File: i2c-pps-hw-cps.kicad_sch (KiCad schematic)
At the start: 36 parts, among them Q1 SiR880BDP, Q2 SiR880BDP, Q3 SiR880BDP, Q4 SiR880BDP, U1 BQ25758S

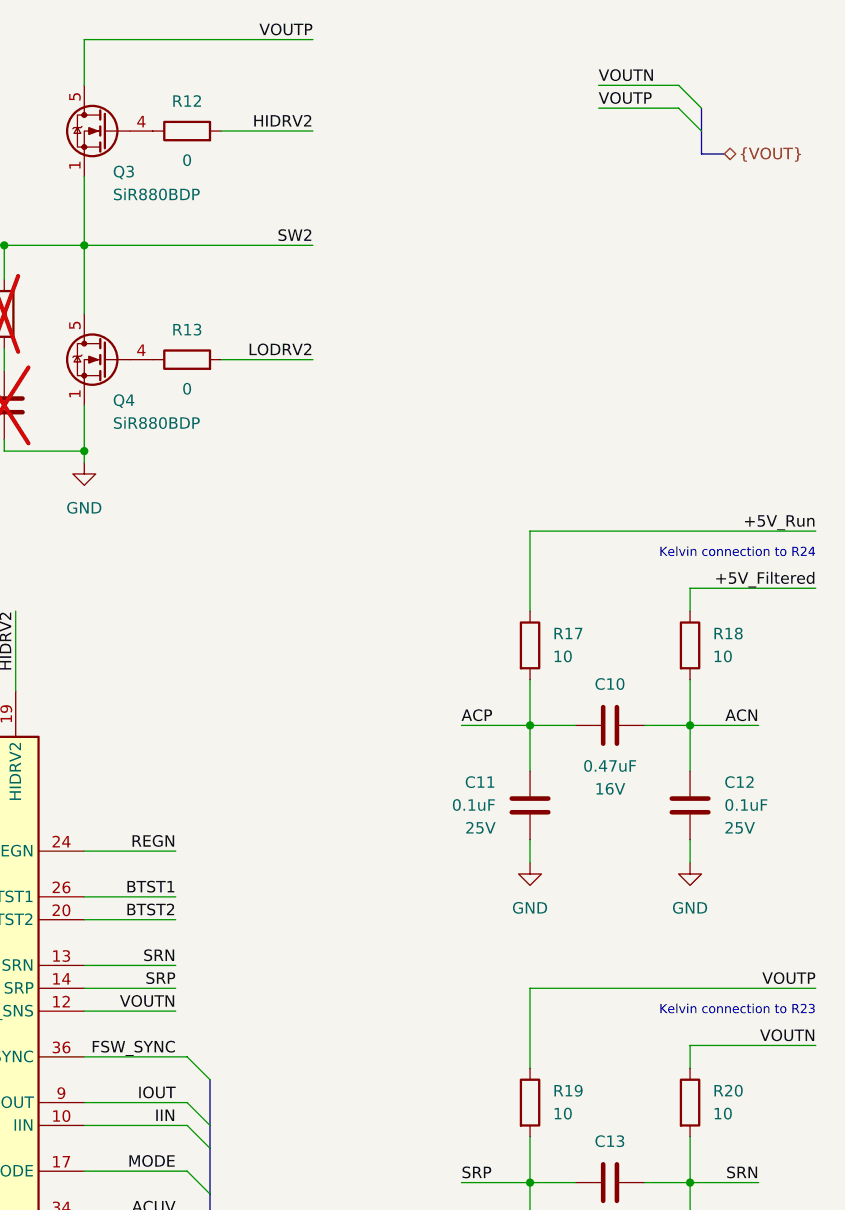
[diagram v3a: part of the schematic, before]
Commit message: Rename VOUTP to VOUT_Switcher for clarity
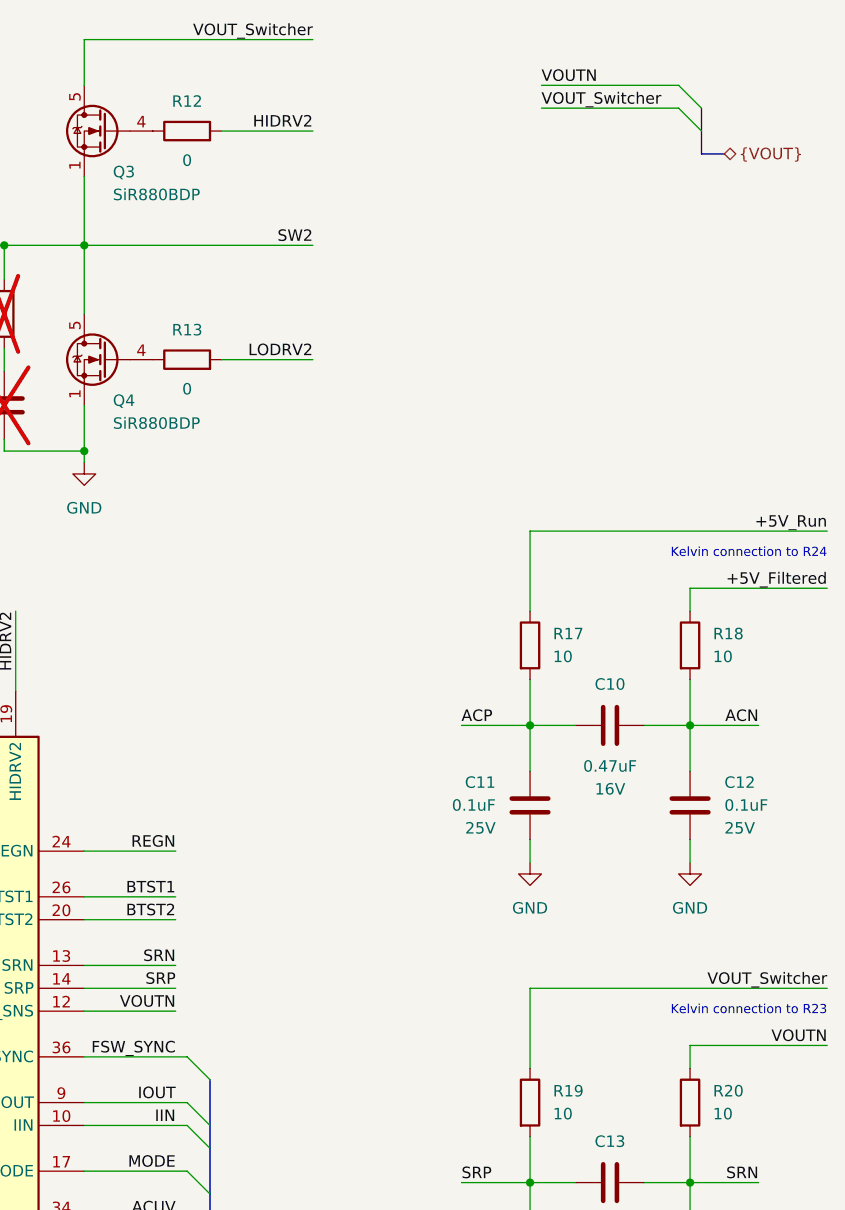
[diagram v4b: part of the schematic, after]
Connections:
- net VOUTP renamed VOUT_Switcher
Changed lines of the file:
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@@
 	)
 	(bus_alias "VOUT"
-		(members "VOUTN" "VOUTP")
+		(members "VOUTN" "VOUT_Switcher")
 	)
 	(text "Kelvin connection to R24"
 		(exclude_from_sim no)
-		(at 238.76 88.9 0)
+		(at 240.03 88.9 0)
 		(effects
 			(font
@@
 	(text "Kelvin connection to R23"
 		(exclude_from_sim no)
-		(at 238.76 139.7 0)
+		(at 240.03 139.7 0)
 		(effects
 			(font
@@
 	(wire
 		(pts
-			(xy 238.76 86.36) (xy 207.01 86.36)
+			(xy 240.03 86.36) (xy 207.01 86.36)
 		)
 		(stroke
@@
 	(wire
 		(pts
+			(xy 207.01 137.16) (xy 240.03 137.16)
+		)
+		(stroke
+			(width 0)
+			(type default)
+		)
+	)
+	(wire
+		(pts
 			(xy 167.64 127) (xy 157.48 127)
 		)
@@
 	(wire
 		(pts
-			(xy 214.63 39.37) (xy 223.52 39.37)
+			(xy 208.28 39.37) (xy 223.52 39.37)
 		)
 		(stroke
@@
 	(wire
 		(pts
-			(xy 238.76 137.16) (xy 207.01 137.16)
-		)
-		(stroke
-			(width 0)
-			(type default)
-		)
-	)
-	(wire
-		(pts
 			(xy 224.79 107.95) (xy 219.71 107.95)
 		)
@@
 	(wire
 		(pts
+			(xy 207.01 137.16) (xy 207.01 146.05)
+		)
+		(stroke
+			(width 0)
+			(type default)
+		)
+	)
+	(wire
+		(pts
 			(xy 157.48 149.86) (xy 168.91 149.86)
 		)
@@
 	(wire
 		(pts
-			(xy 214.63 36.83) (xy 223.52 36.83)
+			(xy 208.28 36.83) (xy 223.52 36.83)
 		)
 		(stroke
@@
 	(wire
 		(pts
-			(xy 207.01 137.16) (xy 207.01 146.05)
-		)
-		(stroke
-			(width 0)
-			(type default)
-		)
-	)
-	(wire
-		(pts
 			(xy 182.88 54.61) (xy 157.48 54.61)
 		)
@@
 	(wire
 		(pts
-			(xy 238.76 92.71) (xy 224.79 92.71)
+			(xy 240.03 92.71) (xy 224.79 92.71)
 		)
 		(stroke
@@
 	(wire
 		(pts
-			(xy 238.76 143.51) (xy 224.79 143.51)
+			(xy 240.03 143.51) (xy 224.79 143.51)
 		)
 		(stroke
@@
 	)
 	(label "VOUTN"
-		(at 214.63 36.83 0)
+		(at 208.28 36.83 0)
 		(effects
 			(font
@@
 	)
 	(label "+5V_Run"
-		(at 238.76 86.36 180)
+		(at 240.03 86.36 180)
 		(effects
 			(font
@@
 		)
 	)
-	(label "VOUTP"
+	(label "VOUT_Switcher"
 		(at 182.88 31.75 180)
 		(effects
@@
 		)
 	)
-	(label "VOUTP"
-		(at 214.63 39.37 0)
+	(label "VOUT_Switcher"
+		(at 208.28 39.37 0)
 		(effects
 			(font
@@
 	)
 	(label "+5V_Filtered"
-		(at 238.76 92.71 180)
+		(at 240.03 92.71 180)
 		(effects
 			(font
@@
 	)
 	(label "VOUTN"
-		(at 238.76 143.51 180)
+		(at 240.03 143.51 180)
 		(effects
 			(font
@@
 		)
 	)
-	(label "VOUTP"
-		(at 238.76 137.16 180)
-		(effects
-			(font
+	(label "VOUT_Switcher"
+		(at 240.03 137.16 180)
+		(effects
+			(font

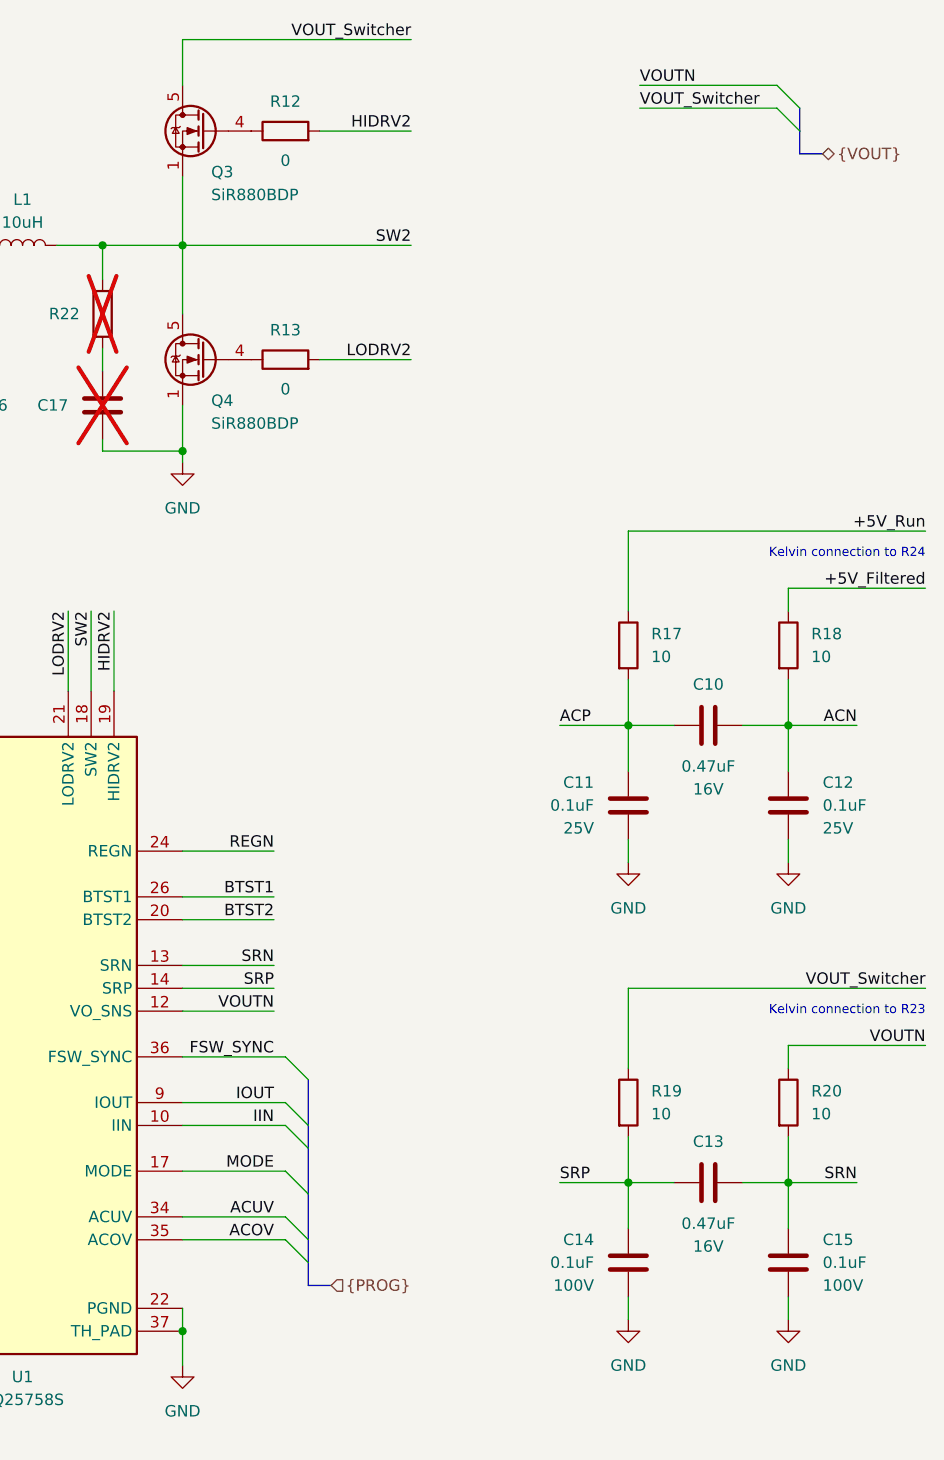
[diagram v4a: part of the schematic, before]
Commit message: Rename VOUTN to VOUT_Filtered for clarity
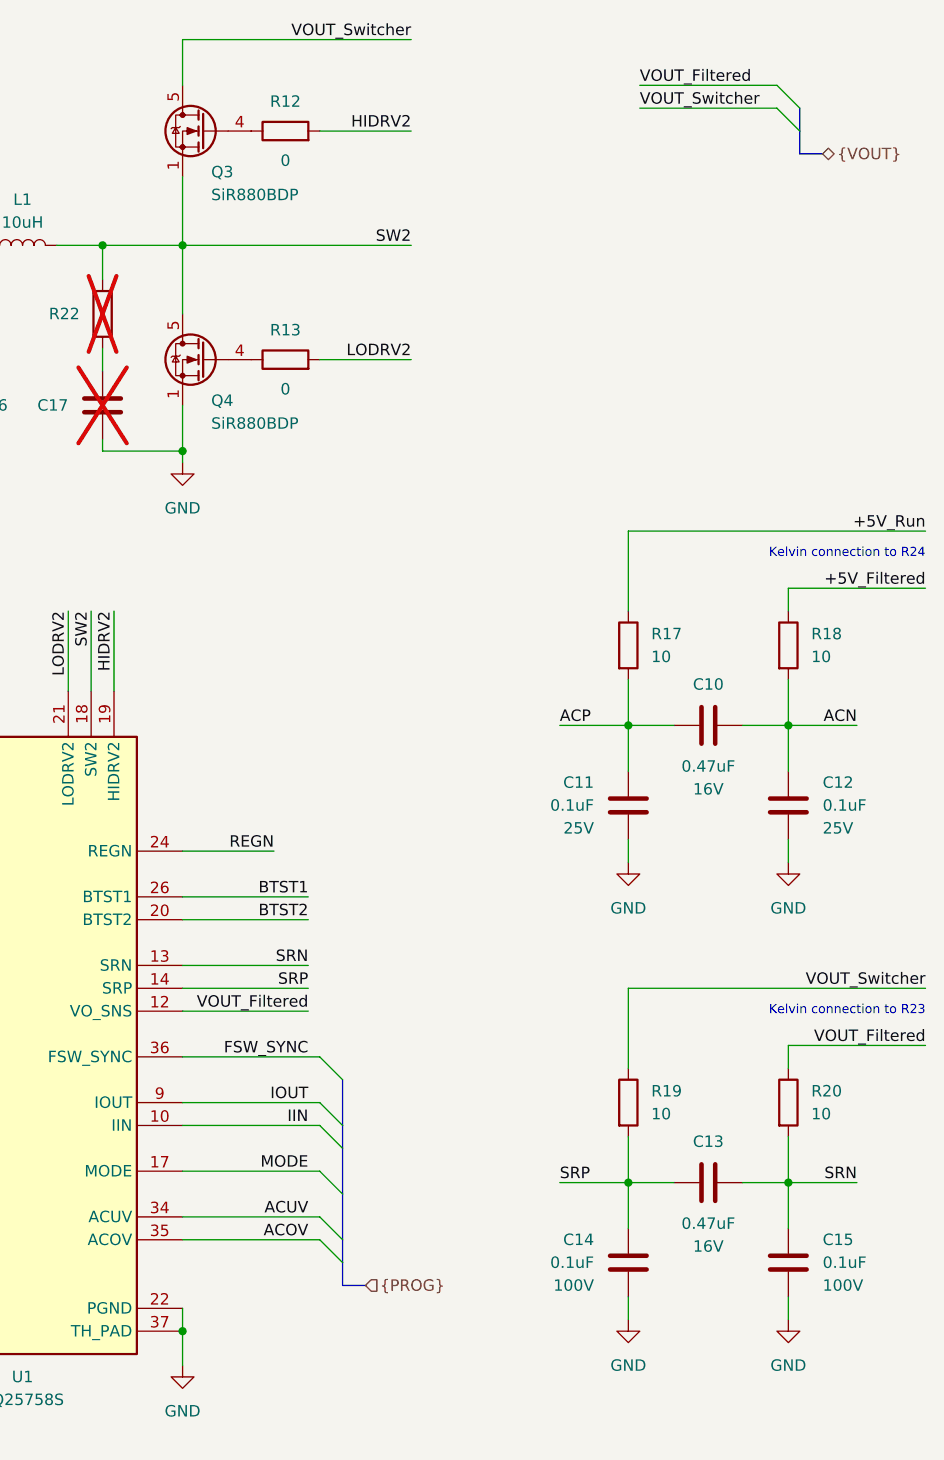
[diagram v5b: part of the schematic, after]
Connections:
- net VOUTN renamed VOUT_Filtered
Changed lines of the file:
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@@
 	)
 	(bus_alias "VOUT"
-		(members "VOUTN" "VOUT_Switcher")
+		(members "VOUT_Filtered" "VOUT_Switcher")
 	)
 	(text "Kelvin connection to R24"
@@
 	)
 	(bus_entry
-		(at 168.91 144.78)
+		(at 172.72 144.78)
 		(size 2.54 2.54)
 		(stroke
@@
 	)
 	(bus_entry
-		(at 168.91 165.1)
+		(at 172.72 165.1)
 		(size 2.54 2.54)
 		(stroke
@@
 	)
 	(bus_entry
-		(at 168.91 157.48)
+		(at 172.72 157.48)
 		(size 2.54 2.54)
 		(stroke
@@
 	)
 	(bus_entry
-		(at 168.91 149.86)
+		(at 172.72 149.86)
 		(size 2.54 2.54)
 		(stroke
@@
 	)
 	(bus_entry
-		(at 168.91 162.56)
+		(at 172.72 162.56)
 		(size 2.54 2.54)
 		(stroke
@@
 	)
 	(bus_entry
-		(at 168.91 152.4)
+		(at 172.72 152.4)
 		(size 2.54 2.54)
 		(stroke
@@
 	(wire
 		(pts
+			(xy 157.48 149.86) (xy 172.72 149.86)
+		)
+		(stroke
+			(width 0)
+			(type default)
+		)
+	)
+	(wire
+		(pts
 			(xy 148.59 54.61) (xy 148.59 58.42)
 		)
@@
 	(bus
 		(pts
-			(xy 171.45 154.94) (xy 171.45 160.02)
+			(xy 175.26 154.94) (xy 175.26 160.02)
 		)
 		(stroke
@@
 	(wire
 		(pts
-			(xy 157.48 157.48) (xy 168.91 157.48)
-		)
-		(stroke
-			(width 0)
-			(type default)
-		)
-	)
-	(wire
-		(pts
 			(xy 157.48 78.74) (xy 157.48 77.47)
 		)
@@
 	(wire
 		(pts
-			(xy 157.48 162.56) (xy 168.91 162.56)
-		)
-		(stroke
-			(width 0)
-			(type default)
-		)
-	)
-	(wire
-		(pts
 			(xy 147.32 95.25) (xy 147.32 104.14)
 		)
@@
 	(bus
 		(pts
-			(xy 171.45 152.4) (xy 171.45 154.94)
+			(xy 175.26 152.4) (xy 175.26 154.94)
 		)
 		(stroke
@@
 	(wire
 		(pts
-			(xy 167.64 134.62) (xy 157.48 134.62)
-		)
-		(stroke
-			(width 0)
-			(type default)
-		)
-	)
-	(wire
-		(pts
 			(xy 82.55 158.75) (xy 69.85 158.75)
 		)
@@
 	(wire
 		(pts
-			(xy 167.64 127) (xy 157.48 127)
-		)
-		(stroke
-			(width 0)
-			(type default)
-		)
-	)
-	(wire
-		(pts
 			(xy 232.41 158.75) (xy 224.79 158.75)
 		)
@@
 	(wire
 		(pts
+			(xy 157.48 144.78) (xy 172.72 144.78)
+		)
+		(stroke
+			(width 0)
+			(type default)
+		)
+	)
+	(wire
+		(pts
 			(xy 208.28 39.37) (xy 223.52 39.37)
 		)
@@
 		)
 	)
-	(wire
-		(pts
-			(xy 167.64 137.16) (xy 157.48 137.16)
-		)
-		(stroke
-			(width 0)
-			(type default)
-		)
-	)
 	(bus
 		(pts
@@
 	(wire
 		(pts
+			(xy 157.48 157.48) (xy 172.72 157.48)
+		)
+		(stroke
+			(width 0)
+			(type default)
+		)
+	)
+	(wire
+		(pts
 			(xy 207.01 153.67) (xy 207.01 158.75)
 		)
@@
 	(wire
 		(pts
-			(xy 157.48 149.86) (xy 168.91 149.86)
+			(xy 157.48 137.16) (xy 171.45 137.16)
+		)
+		(stroke
+			(width 0)
+			(type default)
+		)
+	)
+	(wire
+		(pts
+			(xy 157.48 129.54) (xy 171.45 129.54)
 		)
 		(stroke
@@
 	(wire
 		(pts
-			(xy 167.64 139.7) (xy 157.48 139.7)
+			(xy 171.45 139.7) (xy 157.48 139.7)
 		)
 		(stroke
@@
 	(bus
 		(pts
-			(xy 171.45 152.4) (xy 171.45 147.32)
+			(xy 175.26 152.4) (xy 175.26 147.32)
 		)
 		(stroke
@@
 	(wire
 		(pts
+			(xy 157.48 152.4) (xy 172.72 152.4)
+		)
+		(stroke
+			(width 0)
+			(type default)
+		)
+	)
+	(wire
+		(pts
 			(xy 39.37 142.24) (xy 54.61 142.24)
 		)
@@
 	(bus
 		(pts
-			(xy 171.45 167.64) (xy 171.45 170.18)
+			(xy 175.26 167.64) (xy 175.26 170.18)
 		)
 		(stroke
@@
 		)
 	)
+	(wire
+		(pts
+			(xy 157.48 134.62) (xy 171.45 134.62)
+		)
+		(stroke
+			(width 0)
+			(type default)
+		)
+	)
 	(bus
 		(pts
-			(xy 171.45 165.1) (xy 171.45 167.64)
+			(xy 175.26 165.1) (xy 175.26 167.64)
 		)
 		(stroke
@@
 	(wire
 		(pts
-			(xy 157.48 144.78) (xy 168.91 144.78)
-		)
-		(stroke
-			(width 0)
-			(type default)
-		)
-	)
-	(wire
-		(pts
 			(xy 172.72 41.91) (xy 182.88 41.91)
 		)
@@
 	(wire
 		(pts
+			(xy 157.48 165.1) (xy 172.72 165.1)
+		)
+		(stroke
+			(width 0)
+			(type default)
+		)
+	)
+	(wire
+		(pts
 			(xy 119.38 132.08) (xy 119.38 129.54)
 		)
@@
 	(wire
 		(pts
+			(xy 157.48 127) (xy 171.45 127)
+		)
+		(stroke
+			(width 0)
+			(type default)
+		)
+	)
+	(wire
+		(pts
 			(xy 157.48 77.47) (xy 157.48 72.39)
 		)
@@
 	(wire
 		(pts
+			(xy 157.48 162.56) (xy 172.72 162.56)
+		)
+		(stroke
+			(width 0)
+			(type default)
+		)
+	)
+	(wire
+		(pts
 			(xy 143.51 54.61) (xy 148.59 54.61)
 		)
@@
 	(wire
 		(pts
-			(xy 167.64 129.54) (xy 157.48 129.54)
-		)
-		(stroke
-			(width 0)
-			(type default)
-		)
-	)
-	(wire
-		(pts
 			(xy 121.92 132.08) (xy 119.38 132.08)
 		)
@@
 	(bus
 		(pts
-			(xy 171.45 160.02) (xy 171.45 165.1)
+			(xy 175.26 160.02) (xy 175.26 165.1)
 		)
 		(stroke
@@
 	(bus
 		(pts
-			(xy 171.45 170.18) (xy 173.99 170.18)
+			(xy 175.26 170.18) (xy 177.8 170.18)
 		)
 		(stroke
@@
 	(wire
 		(pts
-			(xy 157.48 152.4) (xy 168.91 152.4)
-		)
-		(stroke
-			(width 0)
-			(type default)
-		)
-	)
-	(wire
-		(pts
 			(xy 182.88 31.75) (xy 157.48 31.75)
 		)
@@
 	(wire
 		(pts
-			(xy 157.48 165.1) (xy 168.91 165.1)
-		)
-		(stroke
-			(width 0)
-			(type default)
-		)
-	)
-	(wire
-		(pts
 			(xy 96.52 31.75) (xy 121.92 31.75)
 		)
@@
 	)
 	(label "SRN"
-		(at 167.64 134.62 180)
+		(at 171.45 134.62 180)
 		(effects
 			(font
@@
 	)
 	(label "FSW_SYNC"
-		(at 167.64 144.78 180)
+		(at 171.45 144.78 180)
 		(effects
 			(font
@@
 		)
 	)
-	(label "VOUTN"
+	(label "VOUT_Filtered"
 		(at 208.28 36.83 0)
 		(effects
@@
 	)
 	(label "MODE"
-		(at 167.64 157.48 180)
+		(at 171.45 157.48 180)
 		(effects
 			(font
@@
 	)
 	(label "IIN"
-		(at 167.64 152.4 180)
+		(at 171.45 152.4 180)
 		(effects
 			(font
@@
 	)
 	(label "ACOV"
-		(at 167.64 165.1 180)
+		(at 171.45 165.1 180)
 		(effects
 			(font
@@
 	)
 	(label "IOUT"
-		(at 167.64 149.86 180)
+		(at 171.45 149.86 180)
 		(effects
 			(font
@@
 	)
 	(label "ACUV"
-		(at 167.64 162.56 180)
+		(at 171.45 162.56 180)
 		(effects
 			(font
@@
 		)
 	)
-	(label "VOUTN"
-		(at 167.64 139.7 180)
+	(label "VOUT_Filtered"
+		(at 171.45 139.7 180)
 		(effects
 			(font
@@
 	)
 	(label "BTST2"
-		(at 167.64 129.54 180)
+		(at 171.45 129.54 180)
 		(effects
 			(font
@@
 	)
 	(label "SRP"
-		(at 167.64 137.16 180)
+		(at 171.45 137.16 180)
 		(effects
 			(font
@@
 		)
 	)
-	(label "VOUTN"
+	(label "VOUT_Filtered"
 		(at 240.03 143.51 180)
 		(effects
@@
 	)
 	(label "BTST1"
-		(at 167.64 127 180)
+		(at 171.45 127 180)
 		(effects
 			(font
@@
 	(hierarchical_label "{PROG}"
 		(shape input)
-		(at 173.99 170.18 0)
-		(effects
-			(font
+		(at 177.8 170.18 0)
+		(effects
+			(font
